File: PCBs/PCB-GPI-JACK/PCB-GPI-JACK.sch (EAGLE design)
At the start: 51 parts, among them IC2 MCP23017SS, X1 DB25F

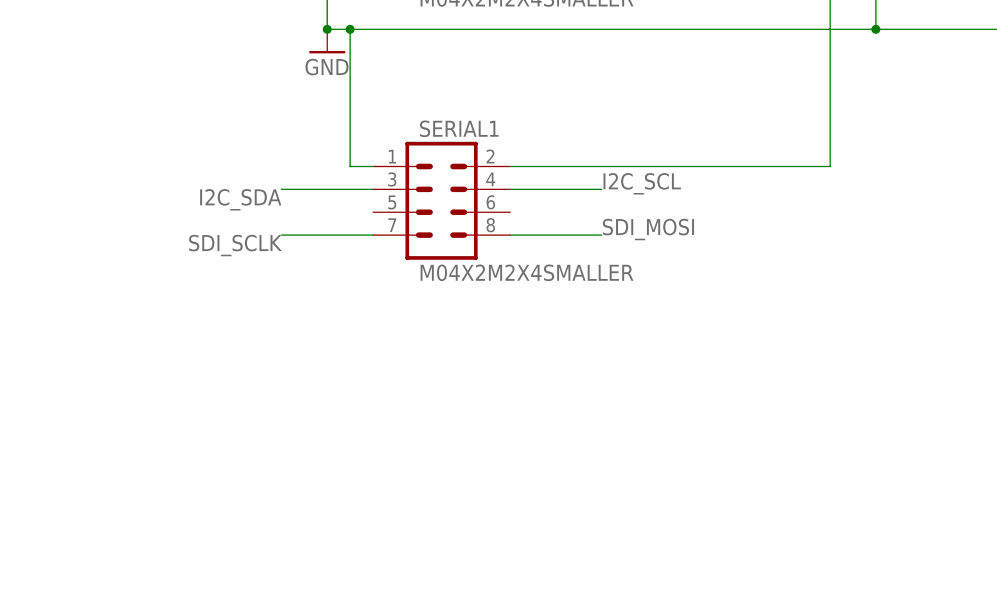
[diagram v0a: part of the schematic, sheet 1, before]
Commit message: size of board
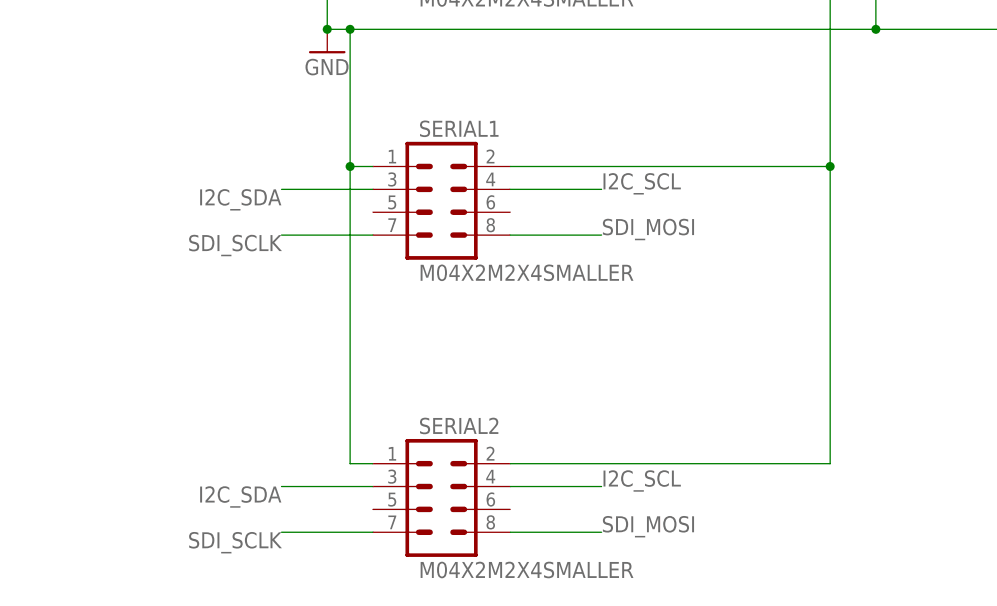
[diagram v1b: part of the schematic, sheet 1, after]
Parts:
- added SERIAL2: M04X2M2X4SMALLER, SKAARHOJ:M04X2M2X4SMALLER
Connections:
- removed net N$2: C6.1, L4.1, SERIAL.2, SERIAL1.2
- new net N$3: C6.1, L4.1, SERIAL.2, SERIAL1.2, SERIAL2.2
- net GND: now also SERIAL2.1
- net I2C_SCL: now also SERIAL2.4
- net I2C_SDA: now also SERIAL2.3
- net SDI_MOSI: now also SERIAL2.8
- net SDI_SCLK: now also SERIAL2.7
